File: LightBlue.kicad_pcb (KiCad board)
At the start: 4 copper layers, 120 x 120 mm, 262 parts, among them J1 Barrel_Jack, J10 Conn_02x04_Odd_Even, J11 Conn_01x02, J12 Conn_01x02, J13 Bus_M.2_Socket_M, J15 Micro_SD_Card_Det, J16 Conn_02x05_Odd_Even, J2 RJ45_LINK-PP_LPJG0926HENL_Hor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, J3 USB_C_Receptacle_USB2.0, J4 USB_A_Stacked, J5 AudioJack, J6 Conn_01x02, J7 HDMI_A_2.0, J8 SiLabs Mini Debug, J9 Conn_Coaxial, M1 Fan_4pin, Q1 DMP3013SFV-7, Q2 BSZ440N10NS3GATMA1, SW1 SW_USER, SW2 SW_WIPE, T1 PA2467NL, U1 RaspberryPi-CM4Lite, U10 TPD4EUSB30, U11 SiliconLabs-MGM210P, U12 PCM5121PW, U13 TLV74033PDBVR, U14 TPD4EUSB30, U15 TPD4EUSB30, U16 BD9D321EFJ, U17 BD9D321EFJ, U18 74LVC1G07, U19 74LVC1G07, U20 LP5569RTWR, U21 PCF85063AT, U22 RT9742GGJ5, U23 TPS23734, U24 TCMT1107, U4 CP2102N-Axx-xQFN20, U5 FSUSB42MUX, U6 FSUSB42MUX, U7 USB2422, U8 TPD4EUSB30, U9 AP2171W, Y1 24MHz, Y2 X32K768S301

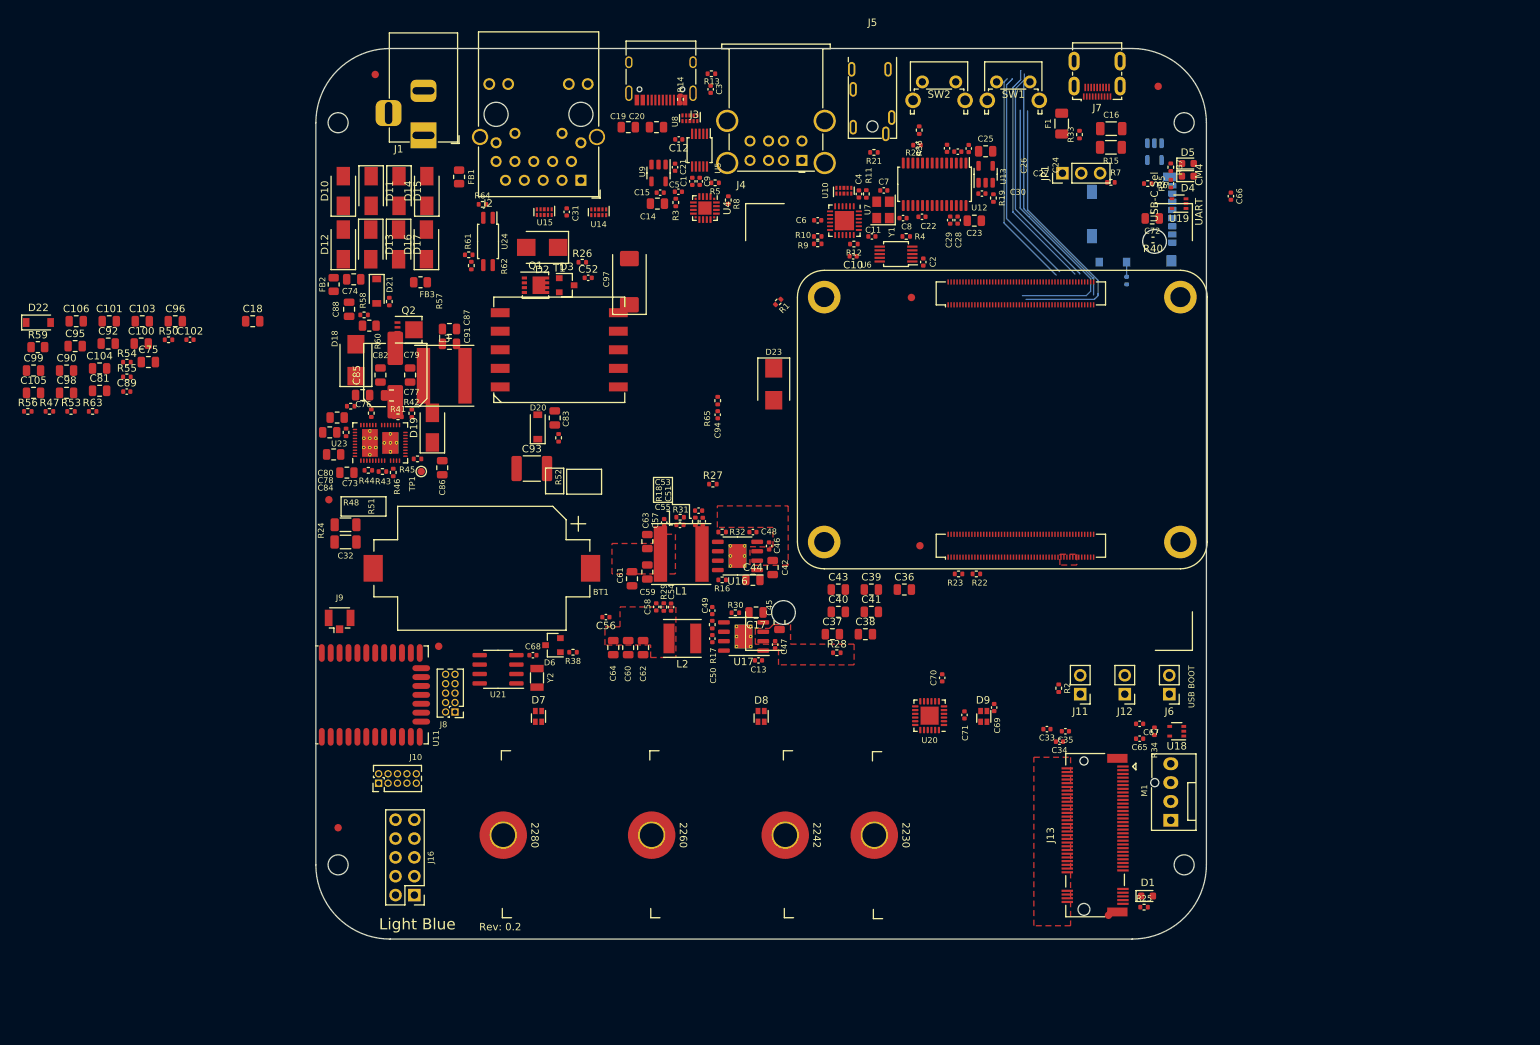
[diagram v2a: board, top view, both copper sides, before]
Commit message: pcb 0.2:
Changes:
Footrints:
-Modified DC Jack to accomodate CUI PJ-002A
-Modified RJ45 to increase clearance between shield and poe pins
-Modified m.2 mounting pads to avoid drc errors
Schematic:
-usb-c facing usb mux is supplied by +3v3VP
-added misc. capacitors
PCB
-min. annular ring for vias set to 0.125 from 0.2

Signed-off-by: Dominik Sliwa <dominik@sliwa.io>
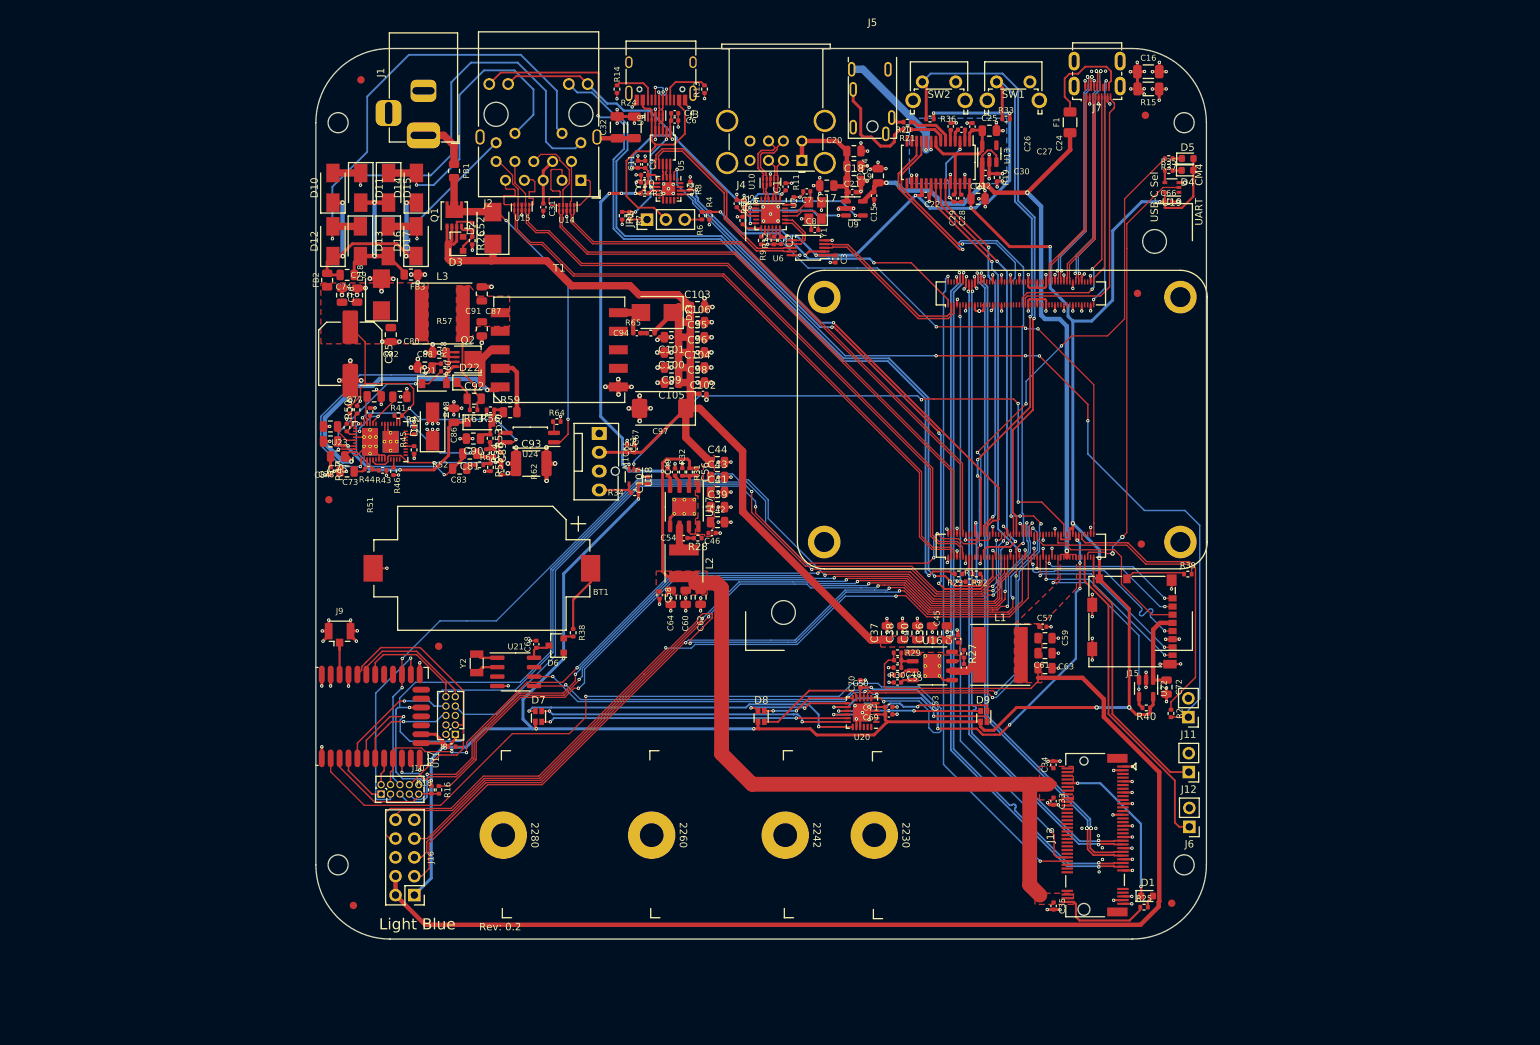
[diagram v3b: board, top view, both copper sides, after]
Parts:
- removed TP1: TestPoint, TestPoint:TestPoint_Pad_D1.0mm
- added C107: 100n, Capacitor_SMD:C_0402_1005Metric, F.Cu at (74.8, 88.2)
- J1: footprint Connector_BarrelJack:BarrelJack_Horizontal -> LightBlue:BarrelJack_CUI_PJ-002A
- J15, R39, U22: moved to F.Cu
- moved M1 93.0 mm to (68.2, 81.9), turned to -90 degrees
- moved C105 86.0 mm to (77.9, 75.0), turned to 180 degrees
- moved C99 86.0 mm to (77.9, 73.0), turned to 180 degrees
- moved C98 85.0 mm to (81.4, 75.0)
- moved C95 83.8 mm to (81.4, 68.9)
- moved C106 83.7 mm to (81.4, 66.9)
- moved C18 83.2 mm to (102.5, 47.9)
- moved U18 80.8 mm to (72.8, 87.7), turned to -90 degrees
- moved C104 80.6 mm to (81.4, 73.0)
- moved C65 78.5 mm to (73.0, 84.0), turned to 90 degrees
- moved C67 78.4 mm to (72.0, 84.0), turned to 90 degrees
- moved R34 77.1 mm to (73.0, 89.8), turned to 0 degrees
- moved C101 75.8 mm to (77.9, 68.9), turned to 180 degrees
- moved C103 74.8 mm to (81.4, 64.8)
- moved U22 72.3 mm to (141.9, 116.2)
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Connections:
- C4 pad 1: +3V3 -> +3.3VP
- C6 pad 1: +3V3 -> +3.3VP
- D6 pad 1: Net-(D6-Pad1) -> +3V3
- D6 pad 2: +3V3 -> Net-(D6-Pad2)
- R38 pad 1: Net-(D6-Pad1) -> Net-(D6-Pad2)
- U23 pad 14: Net-(TP1-Pad1) -> unconnected-(U23-Pad14)
- U5 pad 1: +3V3 -> +3.3VP
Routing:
- net +3V3: track 0.00 -> 435.5 mm, vias 0 -> 20
- net +5V: track 0.00 -> 276.0 mm, vias 0 -> 4
- net GND: track 64.2 -> 295.0 mm, vias 0 -> 270
- net +3.3VP: track 0.00 -> 193.8 mm, vias 0 -> 6
- net /SDA: track 0.00 -> 161.1 mm, vias 0 -> 7
- net +12V: track 0.00 -> 159.0 mm
- net /SCL: track 0.00 -> 155.5 mm, vias 0 -> 6
- net /802.15.4 Radio/Radio.~RESET: track 0.00 -> 138.6 mm, vias 0 -> 2
- net /802.15.4 Radio/Radio.RTS: track 0.00 -> 137.4 mm, vias 0 -> 4
- net /802.15.4 Radio/Radio.CTS: track 0.00 -> 125.8 mm, vias 0 -> 5
- net /CM4/RESET_CM4: track 0.00 -> 125.7 mm, vias 0 -> 5
- net /802.15.4 Radio/Radio.SWDIO: track 0.00 -> 125.3 mm, vias 0 -> 4
- net /802.15.4 Radio/Radio.SWCLK: track 0.00 -> 123.1 mm, vias 0 -> 2
- net Net-(J2-Pad18): track 0.00 -> 119.1 mm, vias 0 -> 2
- net /CM4/GPIO15: track 0.00 -> 115.5 mm, vias 0 -> 2
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- added copper zone on F.Cu, net +48V
- added copper zone on F.Cu, net /PoE/N1A
- added copper zone on In1.Cu, net GND1
- added copper zone on B.Cu, net GNDA
- added copper zone on In2.Cu, net VSS
- removed copper zone on In2.Cu, net GND1
- removed copper zone on In1.Cu, net VSS
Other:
- board text removed: "USB BOOT"

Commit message: Update silkscreen/adjust reference designators
Order some relevant reference designator. Use JP for all jumpers. Place
silkcreen neatly. Add some custom silk screen. Remove heat sink corner
marks on silk screen.

Signed-off-by: Stefan Agner <stefan@agner.ch>
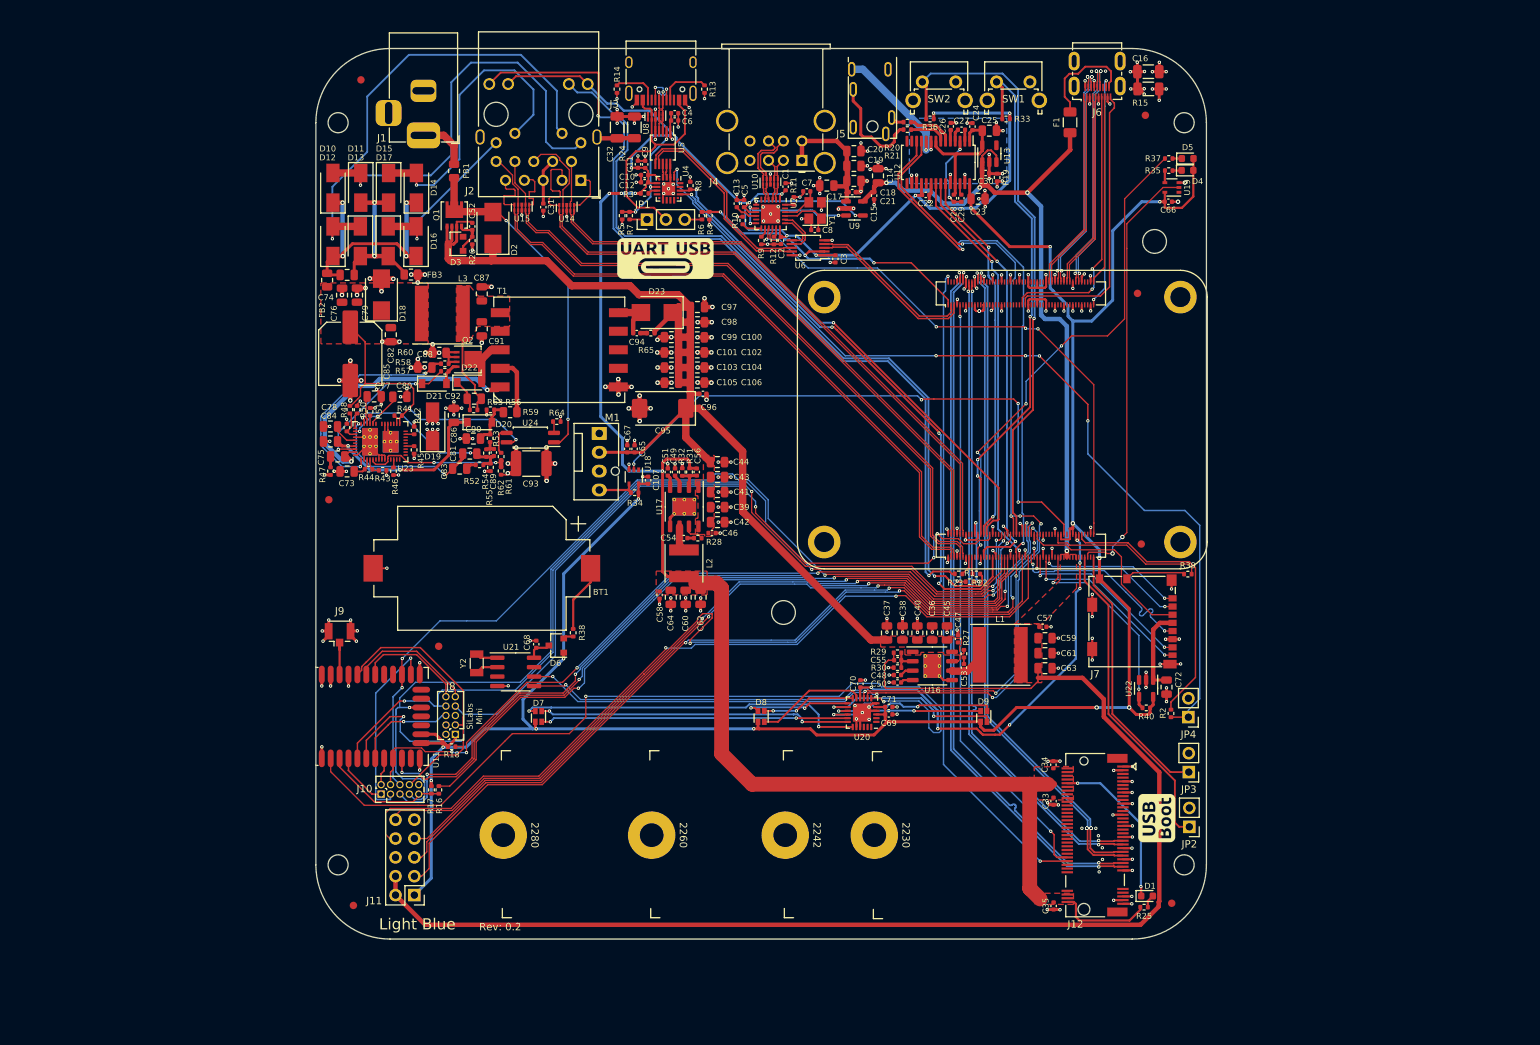
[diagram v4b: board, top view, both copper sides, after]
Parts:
- added Ref**: Val**, LightBlue:SilkScreen_UART-USB-Mux, F.Cu at (77.1, 58.3)
- added Ref**: Val**, LightBlue:SilkScreen_USB-Boot, F.Cu at (143.3, 133.7)
- moved HS1 42.4 mm to (88.0, 111.0)
- renumbered C95 to C100, C100 to C101, C96 to C102, C99 to C103, C98 to C106, C97 to C95, C102 to C96, C103 to C97, C106 to C98, C101 to C99, J16 to J11, J13 to J12, J7 to J6, J15 to J7, J6 to JP2, J12 to JP3, J11 to JP4
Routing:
- net +3.3VP: track 193.8 -> 194.3 mm
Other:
- board text added: "SiLabs Mini"
- board text removed: "CM4"
- board text removed: "UART"
- board text removed: "USB-C Sel"

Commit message: pcb fixups and cleanup
-Moved 5V dcdc converter to clear the heatsink and the LED
-adjusted gnd plane around the radio module

Signed-off-by: Dominik Sliwa <dominik@sliwa.io>
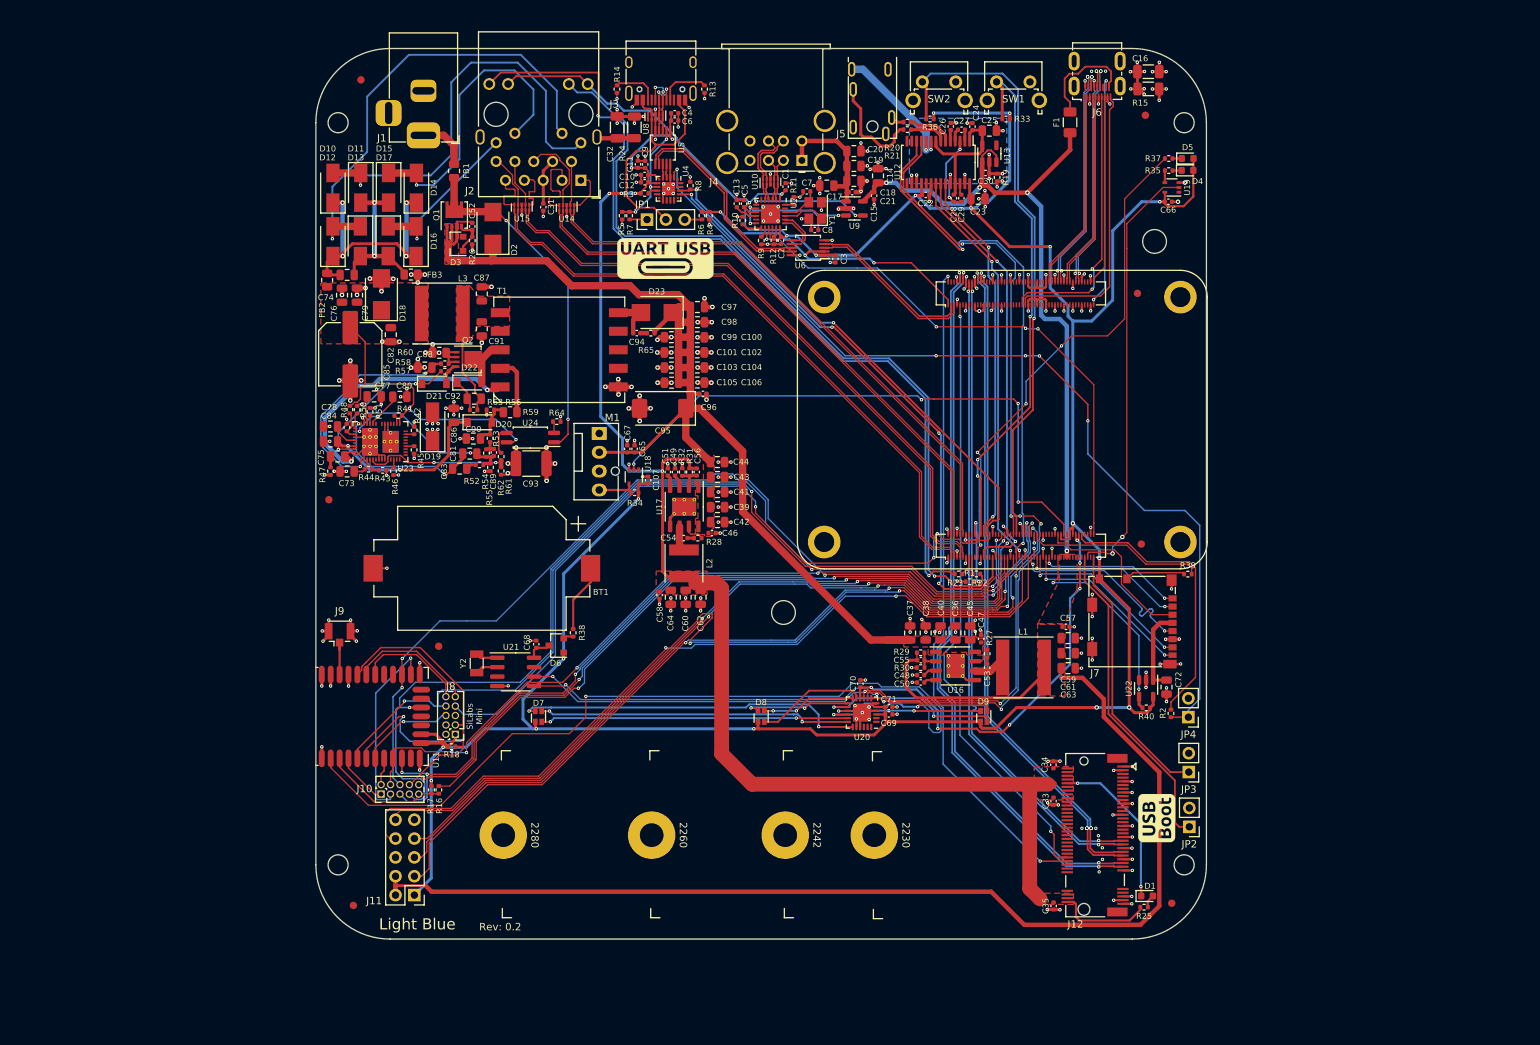
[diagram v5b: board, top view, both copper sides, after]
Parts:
- moved L1 3.56 mm to (125.3, 113.4)
- moved C36 3.12 mm to (116.2, 108.8)
- moved C37 3.12 mm to (110.1, 108.8)
- moved C38 3.12 mm to (112.2, 108.8)
- moved C40 3.12 mm to (114.2, 108.8)
- moved C45 3.12 mm to (118.2, 108.8)
- moved C47 3.12 mm to (119.7, 109.5)
- moved C48 3.12 mm to (111.5, 114.4)
- moved C50 3.12 mm to (111.5, 115.4)
- moved C53 3.12 mm to (120.5, 113.4)
- moved C55 3.12 mm to (111.5, 112.4)
- moved C59 3.12 mm to (131.4, 109.5)
- moved C61 3.12 mm to (131.4, 111.5)
- moved C63 3.12 mm to (131.4, 113.5)
- moved R27 3.12 mm to (120.5, 111.5)
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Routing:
- net +12V: track 159.0 -> 165.3 mm
- net +5V: track 276.0 -> 273.5 mm
- net /SDA: track 161.1 -> 163.5 mm
- net /SCL: track 155.5 -> 157.6 mm
- net /CM4/PCIe.~RST: track 82.6 -> 84.4 mm
- net /CM4/PCIe.CLK+: track 96.1 -> 97.7 mm
- net GND: track 295.0 -> 296.3 mm, vias 270 -> 271
- net +3V3: track 435.5 -> 434.4 mm
- net /CM4/PCIe.~CLKREQ: track 88.9 -> 90.0 mm
- net /CM4/PCIe.CLK-: track 96.1 -> 97.1 mm
- net /802.15.4 Radio/Radio.SWO: track 13.5 -> 12.7 mm
- net /802.15.4 Radio/Radio.SWDIO: track 125.3 -> 124.5 mm
- net /802.15.4 Radio/Radio.TXD: track 111.0 -> 111.6 mm
